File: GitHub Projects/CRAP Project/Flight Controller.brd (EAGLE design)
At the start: 40 x 75 mm, 75 parts, among them J1 2POS_SCREWTERM, J2 4POS_SCREWTERM, Q101 IPD042P03L3G, Q102 IPD042P03L3G

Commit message: Modules, aesthetics, library fixes
1. Renamed Ordnance to Ordnance Power. Moved Firing chains from inside
this module to the top level schematic.
2. Added Breakwire module with pins. Nothing done inside the module
3. Added IMU module with pins. Nothing done inside the module
4. Increased soldermask expansion on TPS63070 per datasheet inside the
Texas.lbr
5. Fixed the header pin names, pin connections, reference designators,
and added a frame on the schematic
6. Got smaller diode array on Ordnance Power board per Evan's request
7. Moved Firing Circuits to top level schematic. Previously on Ordnance
Board
8. Grouped like items on the top level schematic and added a frame for
aesthetics and ease to finding components
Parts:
- removed ORDNANCE:FIRING_CIRCUIT1:R1, ORDNANCE:FIRING_CIRCUIT1:R2, ORDNANCE:FIRING_CIRCUIT1:R3, ORDNANCE:FIRING_CIRCUIT1:R4, ORDNANCE:FIRING_CIRCUIT2:R1, ORDNANCE:FIRING_CIRCUIT2:R2, ORDNANCE:FIRING_CIRCUIT2:R3, ORDNANCE:FIRING_CIRCUIT2:R4, ORDNANCE:FIRING_CIRCUIT3:R1, ORDNANCE:FIRING_CIRCUIT3:R2, ORDNANCE:FIRING_CIRCUIT3:R3, ORDNANCE:FIRING_CIRCUIT3:R4, ORDNANCE:FIRING_CIRCUIT4:R1, ORDNANCE:FIRING_CIRCUIT4:R2, ORDNANCE:FIRING_CIRCUIT4:R3, ORDNANCE:FIRING_CIRCUIT4:R4: 10 k, rcl:R0603
- removed ORDNANCE:FIRING_CIRCUIT1:U$1, ORDNANCE:FIRING_CIRCUIT2:U$1, ORDNANCE:FIRING_CIRCUIT3:U$1, ORDNANCE:FIRING_CIRCUIT4:U$1: PMF170XP, transistor-power:SOT323
- removed ORDNANCE:FIRING_CIRCUIT1:U$2, ORDNANCE:FIRING_CIRCUIT2:U$2, ORDNANCE:FIRING_CIRCUIT3:U$2, ORDNANCE:FIRING_CIRCUIT4:U$2: DMG4800LSD, transistor-power:SO-08
- added FIRING_CIRCUIT1:R1, FIRING_CIRCUIT1:R2, FIRING_CIRCUIT1:R3, FIRING_CIRCUIT1:R4, FIRING_CIRCUIT2:R1, FIRING_CIRCUIT2:R2, FIRING_CIRCUIT2:R3, FIRING_CIRCUIT2:R4, FIRING_CIRCUIT3:R1, FIRING_CIRCUIT3:R2, FIRING_CIRCUIT3:R3, FIRING_CIRCUIT3:R4, FIRING_CIRCUIT4:R1, FIRING_CIRCUIT4:R2, FIRING_CIRCUIT4:R3, FIRING_CIRCUIT4:R4: 10 k, rcl:R0603
- added FIRING_CIRCUIT1:U$1, FIRING_CIRCUIT2:U$1, FIRING_CIRCUIT3:U$1, FIRING_CIRCUIT4:U$1: PMF170XP, transistor-power:SOT323
- added FIRING_CIRCUIT1:U$2, FIRING_CIRCUIT2:U$2, FIRING_CIRCUIT3:U$2, FIRING_CIRCUIT4:U$2: DMG4800LSD, transistor-power:SO-08
- added J3, J4: 4POS_SCREWTERM, CRAP Parts:4POS_0.1
- D301: value STPS3045C -> RB095BM-30; device diode:TO263AB -> diode:TO252
- moved D301 293.0 mm to (-126.0, -228.0)
- moved J1 200.8 mm to (-128.0, -215.0)
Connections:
- net ORDNANCE:!SHDN renamed ORDNANCE_POWER:!SHDN
- net ORDNANCE:N$1 renamed ORDNANCE_POWER:N$1
- net ORDNANCE:N$10 renamed ORDNANCE_POWER:N$10
- net ORDNANCE:N$2 renamed ORDNANCE_POWER:N$2
- net ORDNANCE:N$4 renamed ORDNANCE_POWER:N$4
- net ORDNANCE:N$5 renamed ORDNANCE_POWER:N$5
- net ORDNANCE:N$6 renamed ORDNANCE_POWER:N$6
- net ORDNANCE:N$8 renamed ORDNANCE_POWER:N$8
- net ORDNANCE:ORD_PWR renamed ORDNANCE_POWER:N$99
- removed net ORDNANCE:FIRING_CIRCUIT1:+3V3: ORDNANCE:FIRING_CIRCUIT1:R4.2, ORDNANCE:FIRING_CIRCUIT1:U$1.3
- removed net ORDNANCE:FIRING_CIRCUIT1:FIRE1: ORDNANCE:FIRING_CIRCUIT1:R3.2, ORDNANCE:FIRING_CIRCUIT1:U$2.2
- removed net ORDNANCE:FIRING_CIRCUIT1:FIRE2: ORDNANCE:FIRING_CIRCUIT1:R2.2, ORDNANCE:FIRING_CIRCUIT1:U$2.4
- removed net ORDNANCE:FIRING_CIRCUIT1:GND: ORDNANCE:FIRING_CIRCUIT1:R2.1, ORDNANCE:FIRING_CIRCUIT1:R3.1, ORDNANCE:FIRING_CIRCUIT1:U$2.3
- removed net ORDNANCE:FIRING_CIRCUIT1:N$1: ORDNANCE:FIRING_CIRCUIT1:U$2.1, ORDNANCE:FIRING_CIRCUIT1:U$2.5, ORDNANCE:FIRING_CIRCUIT1:U$2.6
- removed net ORDNANCE:FIRING_CIRCUIT1:N$2: ORDNANCE:FIRING_CIRCUIT1:U$2.7, ORDNANCE:FIRING_CIRCUIT1:U$2.8
- removed net ORDNANCE:FIRING_CIRCUIT1:N$3: ORDNANCE:FIRING_CIRCUIT1:R1.1
- removed net ORDNANCE:FIRING_CIRCUIT1:N$6: ORDNANCE:FIRING_CIRCUIT1:R1.2, ORDNANCE:FIRING_CIRCUIT1:U$1.1
- removed net ORDNANCE:FIRING_CIRCUIT1:N$7: ORDNANCE:FIRING_CIRCUIT1:R4.1, ORDNANCE:FIRING_CIRCUIT1:U$1.2
- removed net ORDNANCE:FIRING_CIRCUIT2:+3V3: ORDNANCE:FIRING_CIRCUIT2:R4.2, ORDNANCE:FIRING_CIRCUIT2:U$1.3
- removed net ORDNANCE:FIRING_CIRCUIT2:FIRE1: ORDNANCE:FIRING_CIRCUIT2:R3.2, ORDNANCE:FIRING_CIRCUIT2:U$2.2
- removed net ORDNANCE:FIRING_CIRCUIT2:FIRE2: ORDNANCE:FIRING_CIRCUIT2:R2.2, ORDNANCE:FIRING_CIRCUIT2:U$2.4
- removed net ORDNANCE:FIRING_CIRCUIT2:GND: ORDNANCE:FIRING_CIRCUIT2:R2.1, ORDNANCE:FIRING_CIRCUIT2:R3.1, ORDNANCE:FIRING_CIRCUIT2:U$2.3
- removed net ORDNANCE:FIRING_CIRCUIT2:N$1: ORDNANCE:FIRING_CIRCUIT2:U$2.1, ORDNANCE:FIRING_CIRCUIT2:U$2.5, ORDNANCE:FIRING_CIRCUIT2:U$2.6
- removed net ORDNANCE:FIRING_CIRCUIT2:N$2: ORDNANCE:FIRING_CIRCUIT2:U$2.7, ORDNANCE:FIRING_CIRCUIT2:U$2.8
- removed net ORDNANCE:FIRING_CIRCUIT2:N$3: ORDNANCE:FIRING_CIRCUIT2:R1.1
- removed net ORDNANCE:FIRING_CIRCUIT2:N$6: ORDNANCE:FIRING_CIRCUIT2:R1.2, ORDNANCE:FIRING_CIRCUIT2:U$1.1
- removed net ORDNANCE:FIRING_CIRCUIT2:N$7: ORDNANCE:FIRING_CIRCUIT2:R4.1, ORDNANCE:FIRING_CIRCUIT2:U$1.2
- removed net ORDNANCE:FIRING_CIRCUIT3:+3V3: ORDNANCE:FIRING_CIRCUIT3:R4.2, ORDNANCE:FIRING_CIRCUIT3:U$1.3
- removed net ORDNANCE:FIRING_CIRCUIT3:FIRE1: ORDNANCE:FIRING_CIRCUIT3:R3.2, ORDNANCE:FIRING_CIRCUIT3:U$2.2
- removed net ORDNANCE:FIRING_CIRCUIT3:FIRE2: ORDNANCE:FIRING_CIRCUIT3:R2.2, ORDNANCE:FIRING_CIRCUIT3:U$2.4
- removed net ORDNANCE:FIRING_CIRCUIT3:GND: ORDNANCE:FIRING_CIRCUIT3:R2.1, ORDNANCE:FIRING_CIRCUIT3:R3.1, ORDNANCE:FIRING_CIRCUIT3:U$2.3
- removed net ORDNANCE:FIRING_CIRCUIT3:N$1: ORDNANCE:FIRING_CIRCUIT3:U$2.1, ORDNANCE:FIRING_CIRCUIT3:U$2.5, ORDNANCE:FIRING_CIRCUIT3:U$2.6
- removed net ORDNANCE:FIRING_CIRCUIT3:N$2: ORDNANCE:FIRING_CIRCUIT3:U$2.7, ORDNANCE:FIRING_CIRCUIT3:U$2.8
- removed net ORDNANCE:FIRING_CIRCUIT3:N$3: ORDNANCE:FIRING_CIRCUIT3:R1.1
- removed net ORDNANCE:FIRING_CIRCUIT3:N$6: ORDNANCE:FIRING_CIRCUIT3:R1.2, ORDNANCE:FIRING_CIRCUIT3:U$1.1
- removed net ORDNANCE:FIRING_CIRCUIT3:N$7: ORDNANCE:FIRING_CIRCUIT3:R4.1, ORDNANCE:FIRING_CIRCUIT3:U$1.2
- removed net ORDNANCE:FIRING_CIRCUIT4:+3V3: ORDNANCE:FIRING_CIRCUIT4:R4.2, ORDNANCE:FIRING_CIRCUIT4:U$1.3
- removed net ORDNANCE:FIRING_CIRCUIT4:FIRE1: ORDNANCE:FIRING_CIRCUIT4:R3.2, ORDNANCE:FIRING_CIRCUIT4:U$2.2
- removed net ORDNANCE:FIRING_CIRCUIT4:FIRE2: ORDNANCE:FIRING_CIRCUIT4:R2.2, ORDNANCE:FIRING_CIRCUIT4:U$2.4
- removed net ORDNANCE:FIRING_CIRCUIT4:GND: ORDNANCE:FIRING_CIRCUIT4:R2.1, ORDNANCE:FIRING_CIRCUIT4:R3.1, ORDNANCE:FIRING_CIRCUIT4:U$2.3
- removed net ORDNANCE:FIRING_CIRCUIT4:N$1: ORDNANCE:FIRING_CIRCUIT4:U$2.1, ORDNANCE:FIRING_CIRCUIT4:U$2.5, ORDNANCE:FIRING_CIRCUIT4:U$2.6
- removed net ORDNANCE:FIRING_CIRCUIT4:N$2: ORDNANCE:FIRING_CIRCUIT4:U$2.7, ORDNANCE:FIRING_CIRCUIT4:U$2.8
- removed net ORDNANCE:FIRING_CIRCUIT4:N$3: ORDNANCE:FIRING_CIRCUIT4:R1.1
- removed net ORDNANCE:FIRING_CIRCUIT4:N$6: ORDNANCE:FIRING_CIRCUIT4:R1.2, ORDNANCE:FIRING_CIRCUIT4:U$1.1
- removed net ORDNANCE:FIRING_CIRCUIT4:N$7: ORDNANCE:FIRING_CIRCUIT4:R4.1, ORDNANCE:FIRING_CIRCUIT4:U$1.2
- removed net ORDNANCE:N$7: D301.K
- new net +12V: D301.3
- net GND: now also FIRING_CIRCUIT1:R2.1, FIRING_CIRCUIT1:R3.1, FIRING_CIRCUIT1:U$2.3, FIRING_CIRCUIT2:R2.1, FIRING_CIRCUIT2:R3.1, FIRING_CIRCUIT2:U$2.3, FIRING_CIRCUIT3:R2.1, FIRING_CIRCUIT3:R3.1, FIRING_CIRCUIT3:U$2.3, FIRING_CIRCUIT4:R2.1, FIRING_CIRCUIT4:R3.1, FIRING_CIRCUIT4:U$2.3

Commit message: Added frames and MPU-9250 into IMU module
Also remade the board again because it broke.
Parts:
- added IMU1:U1: (no value), InvenSense:QFN-24
- moved J1 421.7 mm to (-26.7, 194.3)
- moved D301 418.5 mm to (-34.3, 180.3)
- moved J4 398.3 mm to (-77.5, 194.3)
- moved J3 387.0 mm to (-59.7, 194.3)
- moved FIRING_CIRCUIT4:R4 334.9 mm to (-30.5, 146.1)
- moved FIRING_CIRCUIT4:R1 310.6 mm to (-40.6, 123.2)
- moved FIRING_CIRCUIT4:R3 306.2 mm to (-78.7, 123.2)
- moved FIRING_CIRCUIT4:R2 301.3 mm to (-59.7, 123.2)
- moved FIRING_CIRCUIT3:R4 298.3 mm to (-30.5, 118.1)
- moved FIRING_CIRCUIT4:U$1 287.1 mm to (-49.5, 144.8)
- moved FIRING_CIRCUIT3:R1 274.6 mm to (-40.6, 95.2)
- moved FIRING_CIRCUIT4:U$2 269.2 mm to (-17.8, 125.7)
- moved FIRING_CIRCUIT3:R3 269.0 mm to (-78.7, 95.2)
- moved FIRING_CIRCUIT3:R2 264.1 mm to (-59.7, 95.2)
- moved FIRING_CIRCUIT3:U$1 263.6 mm to (-49.5, 116.8)
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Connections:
- removed net DCDC_REGULATOR:GND: C101.2, C102.2, C103.2, C104.2, C105.2, C106.2, C107.2, C108.2, C109.2, C110.2, C111.2, Q101.1, R104.1, U$101.P$10, U$101.P$15, U$101.P$4, U$101.P$6
- new net FIRING_CIRCUIT1:+3V3: FIRING_CIRCUIT1:R4.2, FIRING_CIRCUIT1:U$1.3
- new net FIRING_CIRCUIT1:FIRE1: FIRING_CIRCUIT1:R3.2, FIRING_CIRCUIT1:U$2.2
- new net FIRING_CIRCUIT1:FIRE2: FIRING_CIRCUIT1:R2.2, FIRING_CIRCUIT1:U$2.4
- new net FIRING_CIRCUIT1:N$1: FIRING_CIRCUIT1:U$2.1, FIRING_CIRCUIT1:U$2.5, FIRING_CIRCUIT1:U$2.6
- new net FIRING_CIRCUIT1:N$2: FIRING_CIRCUIT1:U$2.7, FIRING_CIRCUIT1:U$2.8
- new net FIRING_CIRCUIT1:N$3: FIRING_CIRCUIT1:R1.1
- new net FIRING_CIRCUIT1:N$6: FIRING_CIRCUIT1:R1.2, FIRING_CIRCUIT1:U$1.1
- new net FIRING_CIRCUIT1:N$7: FIRING_CIRCUIT1:R4.1, FIRING_CIRCUIT1:U$1.2
- new net FIRING_CIRCUIT2:+3V3: FIRING_CIRCUIT2:R4.2, FIRING_CIRCUIT2:U$1.3
- new net FIRING_CIRCUIT2:FIRE1: FIRING_CIRCUIT2:R3.2, FIRING_CIRCUIT2:U$2.2
- new net FIRING_CIRCUIT2:FIRE2: FIRING_CIRCUIT2:R2.2, FIRING_CIRCUIT2:U$2.4
- new net FIRING_CIRCUIT2:N$1: FIRING_CIRCUIT2:U$2.1, FIRING_CIRCUIT2:U$2.5, FIRING_CIRCUIT2:U$2.6
- new net FIRING_CIRCUIT2:N$2: FIRING_CIRCUIT2:U$2.7, FIRING_CIRCUIT2:U$2.8
- new net FIRING_CIRCUIT2:N$3: FIRING_CIRCUIT2:R1.1
- new net FIRING_CIRCUIT2:N$6: FIRING_CIRCUIT2:R1.2, FIRING_CIRCUIT2:U$1.1
- new net FIRING_CIRCUIT2:N$7: FIRING_CIRCUIT2:R4.1, FIRING_CIRCUIT2:U$1.2
- new net FIRING_CIRCUIT3:+3V3: FIRING_CIRCUIT3:R4.2, FIRING_CIRCUIT3:U$1.3
- new net FIRING_CIRCUIT3:FIRE1: FIRING_CIRCUIT3:R3.2, FIRING_CIRCUIT3:U$2.2
- new net FIRING_CIRCUIT3:FIRE2: FIRING_CIRCUIT3:R2.2, FIRING_CIRCUIT3:U$2.4
- new net FIRING_CIRCUIT3:N$1: FIRING_CIRCUIT3:U$2.1, FIRING_CIRCUIT3:U$2.5, FIRING_CIRCUIT3:U$2.6
- new net FIRING_CIRCUIT3:N$2: FIRING_CIRCUIT3:U$2.7, FIRING_CIRCUIT3:U$2.8
- new net FIRING_CIRCUIT3:N$3: FIRING_CIRCUIT3:R1.1
- new net FIRING_CIRCUIT3:N$6: FIRING_CIRCUIT3:R1.2, FIRING_CIRCUIT3:U$1.1
- new net FIRING_CIRCUIT3:N$7: FIRING_CIRCUIT3:R4.1, FIRING_CIRCUIT3:U$1.2
- new net FIRING_CIRCUIT4:+3V3: FIRING_CIRCUIT4:R4.2, FIRING_CIRCUIT4:U$1.3
- new net FIRING_CIRCUIT4:FIRE1: FIRING_CIRCUIT4:R3.2, FIRING_CIRCUIT4:U$2.2
- new net FIRING_CIRCUIT4:FIRE2: FIRING_CIRCUIT4:R2.2, FIRING_CIRCUIT4:U$2.4
- new net FIRING_CIRCUIT4:N$1: FIRING_CIRCUIT4:U$2.1, FIRING_CIRCUIT4:U$2.5, FIRING_CIRCUIT4:U$2.6
- new net FIRING_CIRCUIT4:N$2: FIRING_CIRCUIT4:U$2.7, FIRING_CIRCUIT4:U$2.8
- new net FIRING_CIRCUIT4:N$3: FIRING_CIRCUIT4:R1.1
- new net FIRING_CIRCUIT4:N$6: FIRING_CIRCUIT4:R1.2, FIRING_CIRCUIT4:U$1.1
- new net FIRING_CIRCUIT4:N$7: FIRING_CIRCUIT4:R4.1, FIRING_CIRCUIT4:U$1.2
- new net IMU1:REGOUT: IMU1:U1.10
- new net IMU1:RESV: IMU1:U1.1
- new net IMU1:RESV/GND: IMU1:U1.20
- new net IMU1:VDD: IMU1:U1.13
- net +3V3: now also IMU1:U1.8, U$101.P7, U$101.P8; no longer U$101.P$7, U$101.P$8
- net DCDC_REGULATOR:N$1: now also U$101.P13; no longer U$101.P$12, U$101.P$13
- net DCDC_REGULATOR:N$10: now also U$101.P5; no longer U$101.P$5
- net DCDC_REGULATOR:N$11: now also U$101.P1, U$101.P14; no longer U$101.P$1, U$101.P$14
- net DCDC_REGULATOR:N$3: now also U$101.P11; no longer U$101.P$11
- net DCDC_REGULATOR:N$5: now also U$101.P9; no longer U$101.P$9
- net DCDC_REGULATOR:N$7: now also U$101.P3; no longer U$101.P$3
- net DCDC_REGULATOR:N$9: now also U$101.P2; no longer U$101.P$2
- net GND: now also C101.2, C102.2, C103.2, C104.2, C105.2, C106.2, C107.2, C108.2, C109.2, C110.2, C111.2, IMU1:U1.18, J1.2, Q101.1, R104.1, U$101.P10, U$101.P15, U$101.P4, U$101.P6; no longer J1.P$2
- net N$6: now also J2.1; no longer J2.P$1
- net N$7: now also J2.2; no longer J2.P$2
- net N$8: now also J2.3; no longer J2.P$3
- net N$9: now also J2.4; no longer J2.P$4
- net VCC_IN: now also J1.1; no longer J1.P$1
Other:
- board size 40 x 75 mm -> 160 x 100 mm

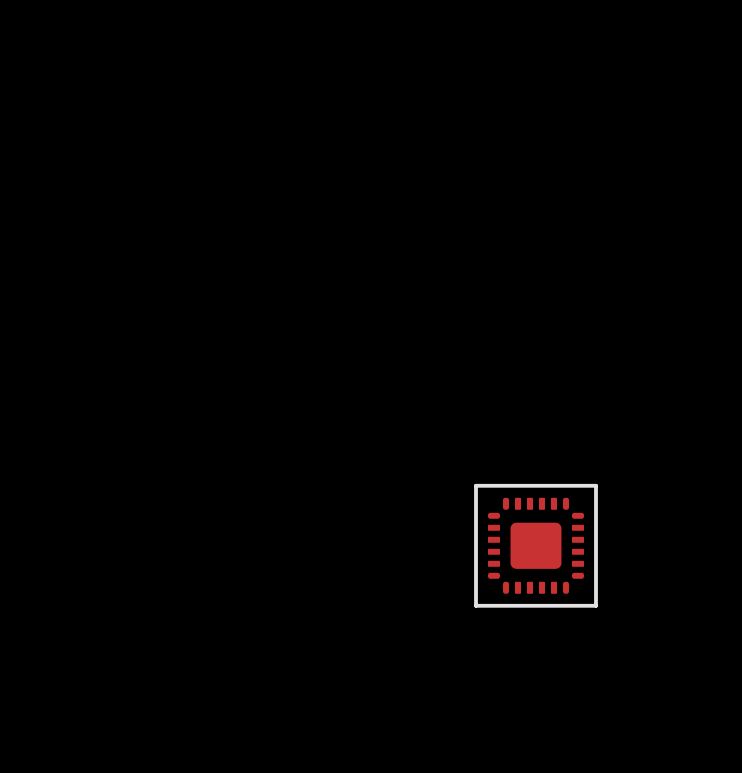
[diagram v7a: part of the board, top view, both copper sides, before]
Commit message: Added Micron 1Gbit memory module
1. Changed all the text to the info layer
2. Added the Micron 1Gbit memory module
3. Routed power and ground to it
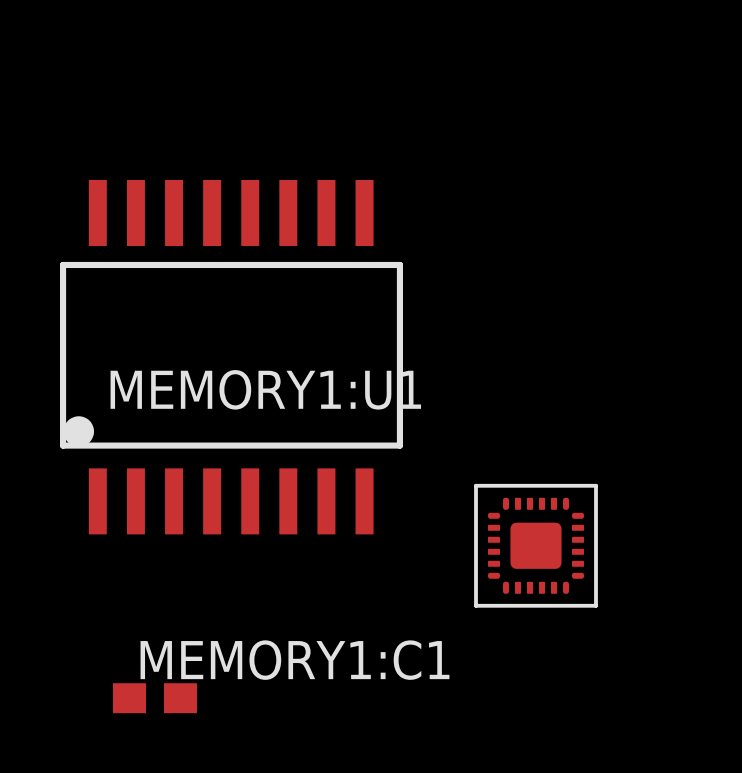
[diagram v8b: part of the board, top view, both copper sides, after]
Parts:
- added MEMORY1:C1: 0.1u, rcl:C0603
- added MEMORY1:U1: (no value), micron:SOP16
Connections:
- new net MEMORY1:+3V3: MEMORY1:C1.1, MEMORY1:U1.2
- new net MEMORY1:GND: MEMORY1:C1.2, MEMORY1:U1.10
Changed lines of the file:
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@@
 </element>
 <element name="IMU1:U1" library="InvenSense" package="QFN-24" value="" x="-97.79" y="-2.54"/>
+<element name="MEMORY1:U1" library="micron" package="SOP16" value="" x="-107.95" y="3.81"/>
+<element name="MEMORY1:C1" library="rcl" package="C0603" value="0.1u" x="-110.49" y="-7.62"/>
 </elements>
 <signals>
@@
 <contactref element="IMU1:U1" pad="20"/>
 </signal>
+<signal name="MEMORY1:GND">
+<contactref element="MEMORY1:U1" pad="10"/>
+<contactref element="MEMORY1:C1" pad="2"/>
+<wire x1="-104.775" y1="8.553" x2="-109.64" y2="-7.62" width="0" layer="19" extent="1-1"/>
+</signal>
+<signal name="MEMORY1:+3V3">
+<contactref element="MEMORY1:U1" pad="2"/>
+<contactref element="MEMORY1:C1" pad="1"/>
+<wire x1="-111.125" y1="-1.06" x2="-111.34" y2="-7.62" width="0" layer="19" extent="1-1"/>
+</signal>
 </signals>
